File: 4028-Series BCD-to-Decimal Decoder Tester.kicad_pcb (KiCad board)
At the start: 2 copper layers, 50 x 45 mm, 33 parts, among them J1 USB_C_Receptacle_USB2.0, SW1 SW_Push, SW2 2MS1T2B2VS2QES, SW3 2MS1T2B2VS2QES, SW4 2MS1T2B2VS2QES, SW5 2MS1T2B2VS2QES, U1 4028

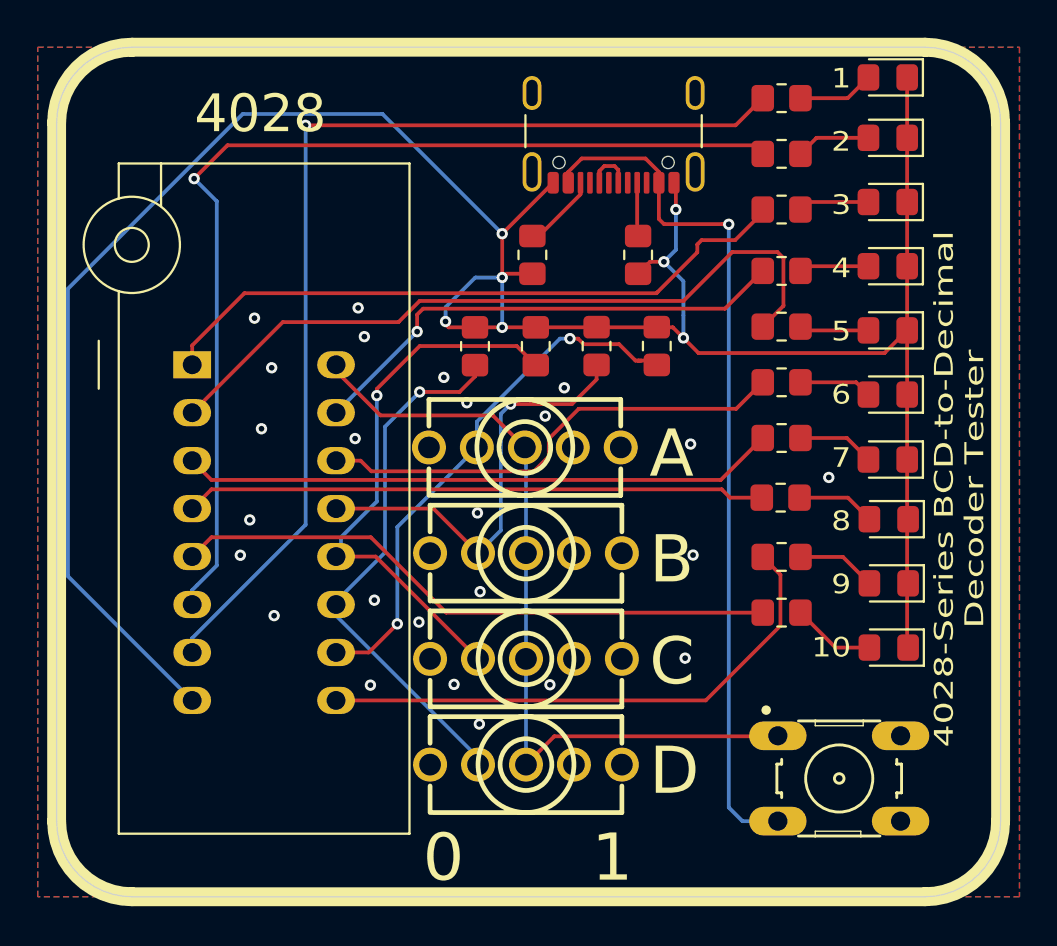
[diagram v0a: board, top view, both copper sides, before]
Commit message: Fixed LED ordering
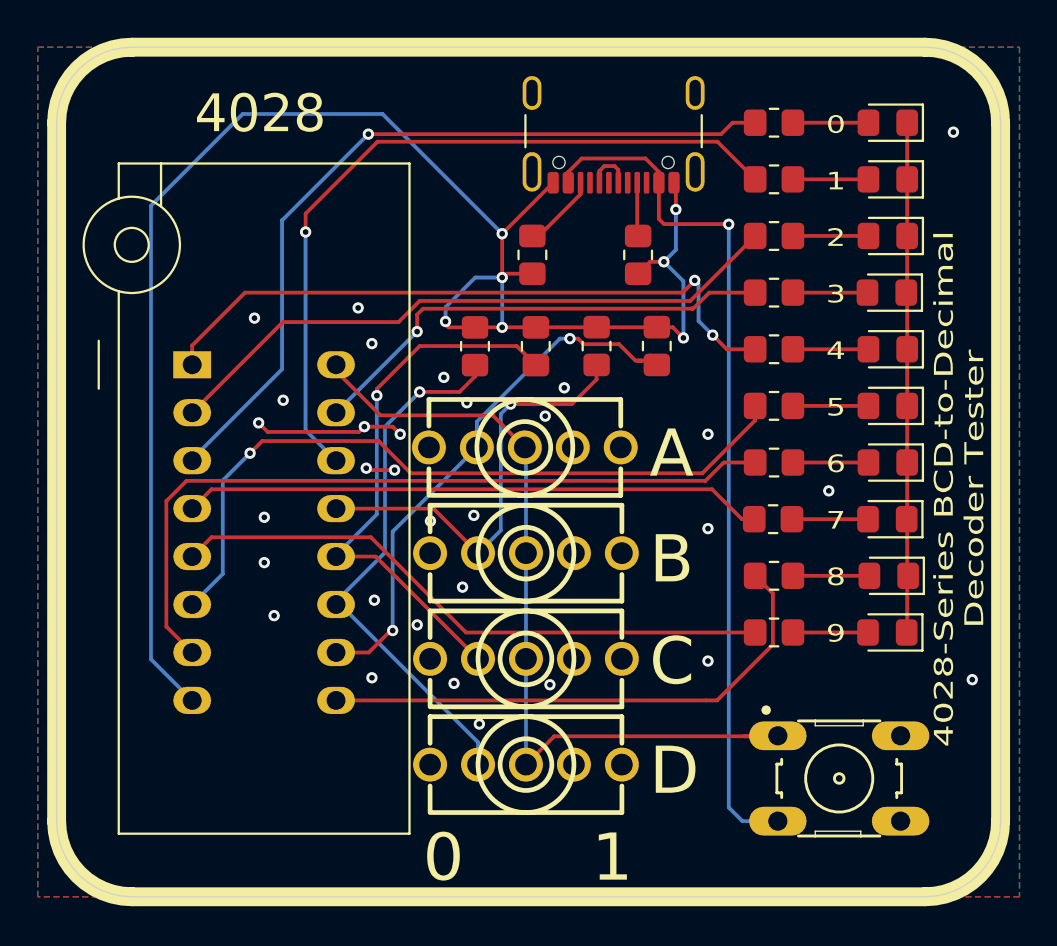
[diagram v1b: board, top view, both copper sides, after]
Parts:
- moved D7 20.4 mm to (143.0, 103.0)
- moved R9 19.3 mm to (137.0, 103.0)
- moved D1 17.8 mm to (143.0, 85.0)
- moved R15 16.7 mm to (137.0, 85.0)
- moved D6 14.2 mm to (143.0, 100.0)
- moved R10 13.4 mm to (137.0, 100.0)
- moved D2 11.4 mm to (143.0, 88.0)
- moved R14 10.8 mm to (137.0, 88.0)
- moved D5 7.80 mm to (143.0, 97.0)
- moved R11 7.41 mm to (137.0, 97.0)
- moved D3 5.00 mm to (143.0, 91.0)
- moved R13 4.82 mm to (137.0, 91.0)
- moved D4 1.40 mm to (143.0, 94.0)
- moved R12 1.22 mm to (137.0, 94.0)
- moved R21 1.21 mm to (136.9, 106.0)
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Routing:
- net Net-(U1-S5): track 54.6 -> 39.6 mm
- net Net-(U1-S1): track 25.3 -> 40.0 mm, vias 0 -> 1
- net Net-(U1-S6): track 55.2 -> 40.6 mm, vias 1 -> 0
- net Net-(U1-S0): track 31.6 -> 41.9 mm, vias 0 -> 1
- net GND: track 135.4 -> 125.3 mm, vias 31 -> 38
- net Net-(U1-S2): track 39.1 -> 33.7 mm
- net Net-(U1-VDD): track 42.8 -> 44.7 mm
- net Net-(U1-S3): track 26.2 -> 25.4 mm
- net Net-(U1-S8): track 29.2 -> 28.4 mm
- net Net-(U1-S4): track 34.7 -> 34.9 mm, vias 0 -> 2
- net (no net): vias 1 -> 0
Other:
- board text added: "0 1 2 3 4 5 6 7 8 9"
- board text removed: "1 2 3 4 5 6 7 8 9 10"
